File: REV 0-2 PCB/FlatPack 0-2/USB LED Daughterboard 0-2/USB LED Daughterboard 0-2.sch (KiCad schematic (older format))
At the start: 60 parts, among them J1 USB_C_Receptacle_USB2.0, J2 Conn_02x05_Odd_Even, Q1 SQJ479EP, U1 STUSB4500, U2 PCA9685PW

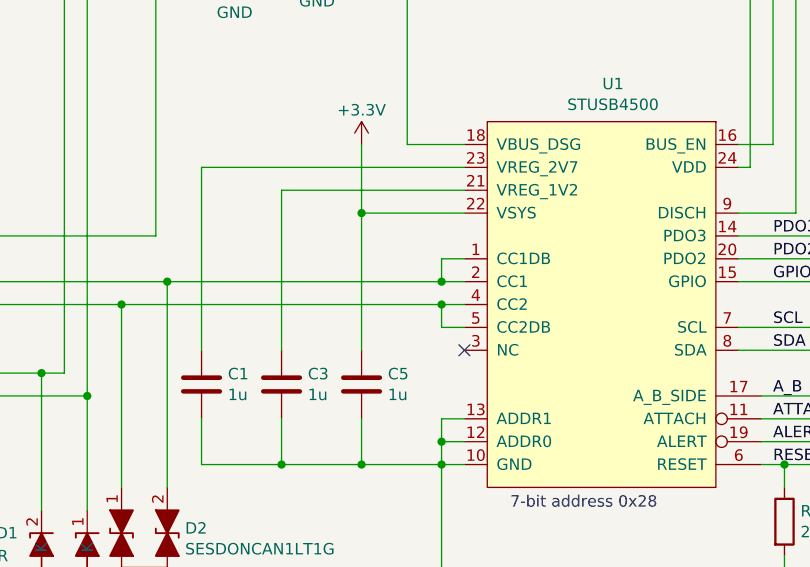
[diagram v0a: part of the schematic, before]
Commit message: More work on USB LED SubBoard
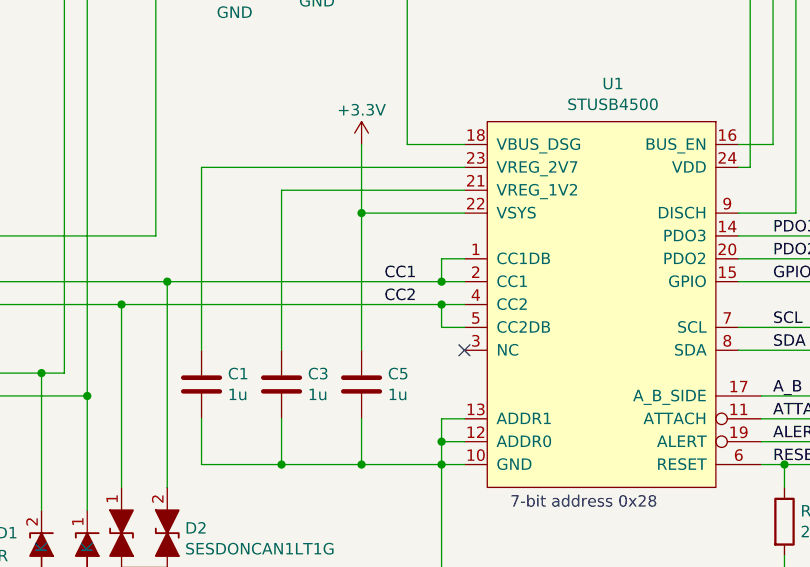
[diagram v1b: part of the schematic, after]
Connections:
- net CC1: now reaches D2.2 (A2), J1.A5 (CC1), U1.1 (CC1DB), U1.2 (CC1)
- net CC2: now reaches D2.1 (A2), J1.B5 (CC2), U1.4 (CC2), U1.5 (CC2DB)
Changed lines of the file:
@@
 Text Label 6100 4900 0    50   ~ 0
 RESET
+Text Label 4400 4100 0    50   ~ 0
+CC1
+Text Label 4400 4200 0    50   ~ 0
+CC2
 $EndSCHEMATC
